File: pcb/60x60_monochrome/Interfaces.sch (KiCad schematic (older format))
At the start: 16 parts, among them J1 Conn_01x05, J10 Conn_01x01_Female, J11 Conn_01x01_Female, J12 Conn_01x01_Female, J13 Conn_01x01_Female, J14 Conn_01x02, J15 Conn_01x04, J2 Conn_01x05, J3 USB_OTG, J4 Conn_01x05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

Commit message: - add pins to the sheets, add reset/boot circuit
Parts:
- D3: footprint Diodes_SMD:D_SOD-123 -> kicad_libraries_new:badger_D_SOD-123_hand
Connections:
- wire segments 65 -> 64
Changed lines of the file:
@@
 I2C_SCL
 $Comp
-L VCC #PWR30
+L VCC #PWR033
 U 1 1 5BD6FE4D
 P 3150 2200
-F 0 "#PWR30" H 3150 2050 50  0001 C CNN
+F 0 "#PWR033" H 3150 2050 50  0001 C CNN
 F 1 "VCC" H 3150 2350 50  0000 C CNN
 F 2 "" H 3150 2200 50  0001 C CNN
@@
 Text Label 4050 2250 3    60   ~ 0
 UART_RX4
-Text Label 3450 2300 3    60   ~ 0
+Text Label 3450 2250 3    60   ~ 0
 UART_TX4
 $Comp
@@
 	3550 2100 3550 2650
 $Comp
-L GND #PWR32
+L GND #PWR034
 U 1 1 5BD6FE74
 P 4300 2150
-F 0 "#PWR32" H 4300 1900 50  0001 C CNN
+F 0 "#PWR034" H 4300 1900 50  0001 C CNN
 F 1 "GND" H 4300 2000 50  0000 C CNN
 F 2 "" H 4300 2150 50  0001 C CNN
@@
 I2C_SCL
 $Comp
-L VCC #PWR31
+L VCC #PWR035
 U 1 1 5BD7123B
 P 3300 5000
-F 0 "#PWR31" H 3300 4850 50  0001 C CNN
+F 0 "#PWR035" H 3300 4850 50  0001 C CNN
 F 1 "VCC" H 3300 5150 50  0000 C CNN
 F 2 "" H 3300 5000 50  0001 C CNN
@@
 	4100 5100 4100 4550
 $Comp
-L GND #PWR33
+L GND #PWR036
 U 1 1 5BD71262
 P 4450 5050
-F 0 "#PWR33" H 4450 4800 50  0001 C CNN
+F 0 "#PWR036" H 4450 4800 50  0001 C CNN
 F 1 "GND" H 4450 4900 50  0000 C CNN
 F 2 "" H 4450 5050 50  0001 C CNN
@@
 	0    -1   -1   0
 $EndComp
-Text Label 5250 3350 2    60   ~ 0
+Text Label 5200 3350 2    60   ~ 0
 UART_TX1
-Text Label 5250 3950 2    60   ~ 0
+Text Label 5200 3950 2    60   ~ 0
 UART_RX1
 Text Label 5250 3550 2    60   ~ 0
 I2C_SCL
 $Comp
-L VCC #PWR34
+L VCC #PWR037
 U 1 1 5BD71F25
 P 5300 4250
-F 0 "#PWR34" H 5300 4100 50  0001 C CNN
+F 0 "#PWR037" H 5300 4100 50  0001 C CNN
 F 1 "VCC" H 5300 4400 50  0000 C CNN
 F 2 "" H 5300 4250 50  0001 C CNN
@@
 	-1   0    0    1
 $EndComp
-Text Label 5250 3750 2    60   ~ 0
+Text Label 5150 3750 2    60   ~ 0
 I2C_SDA
 Text Label 2350 3300 0    60   ~ 0
@@
 I2C_SCL
 $Comp
-L VCC #PWR29
+L VCC #PWR038
 U 1 1 5BD71F2F
 P 2300 4200
-F 0 "#PWR29" H 2300 4050 50  0001 C CNN
+F 0 "#PWR038" H 2300 4050 50  0001 C CNN
 F 1 "VCC" H 2300 4350 50  0000 C CNN
 F 2 "" H 2300 4200 50  0001 C CNN
@@
 	5400 3550 4850 3550
 Wire Wire Line
-	5400 3350 4850 3350
+	4650 3350 5400 3350
 Wire Wire Line
 	5400 3150 5350 3150
@@
 Connection ~ 5300 4050
 Wire Wire Line
-	5400 3950 4850 3950
-Wire Wire Line
-	5400 3750 4850 3750
+	4700 3950 5400 3950
+Wire Wire Line
+	4600 3750 5400 3750
 Wire Wire Line
 	2200 3500 2750 3500
@@
 	5400 3850 4850 3850
 Wire Wire Line
-	5400 3450 4900 3450
-Wire Wire Line
-	4900 3450 4900 3500
-$Comp
-L GND #PWR35
+	4750 3450 5400 3450
+$Comp
+L GND #PWR039
 U 1 1 5BD71F73
 P 5350 3100
-F 0 "#PWR35" H 5350 2850 50  0001 C CNN
+F 0 "#PWR039" H 5350 2850 50  0001 C CNN
 F 1 "GND" H 5350 2950 50  0000 C CNN
 F 2 "" H 5350 3100 50  0001 C CNN
@@
 $EndComp
 $Comp
-L GND #PWR28
+L GND #PWR040
 U 1 1 5BD71F79
 P 2250 3050
-F 0 "#PWR28" H 2250 2800 50  0001 C CNN
+F 0 "#PWR040" H 2250 2800 50  0001 C CNN
 F 1 "GND" H 2250 2900 50  0000 C CNN
 F 2 "" H 2250 3050 50  0001 C CNN
@@
 F 0 "D3" H 9800 1750 50  0000 C CNN
 F 1 "Shottky" H 9800 1550 50  0000 C CNN
-F 2 "Diodes_SMD:D_SOD-123" H 9800 1650 50  0001 C CNN
+F 2 "kicad_libraries_new:badger_D_SOD-123_hand" H 9800 1650 50  0001 C CNN
 F 3 "" H 9800 1650 50  0000 C CNN
 	1    9800 1650
 	-1   0    0    1
 $EndComp
-Text Label 9750 1850 0    60   ~ 0
-USB_DP
-Text Label 9750 1950 0    60   ~ 0
-USB_DM
-$Comp
-L +5V #PWR37
+$Comp
+L +5V #PWR041
 U 1 1 5BD73B57
 P 10000 1600
-F 0 "#PWR37" H 10000 1450 50  0001 C CNN
+F 0 "#PWR041" H 10000 1450 50  0001 C CNN
 F 1 "+5V" H 10000 1740 50  0000 C CNN
 F 2 "" H 10000 1600 50  0001 C CNN
@@
 $EndComp
 $Comp
-L +3.3V #PWR38
+L +3.3V #PWR042
 U 1 1 5BD73B6C
 P 9600 3100
-F 0 "#PWR38" H 9600 2950 50  0001 C CNN
+F 0 "#PWR042" H 9600 2950 50  0001 C CNN
 F 1 "+3.3V" H 9600 3240 50  0000 C CNN
 F 2 "" H 9600 3100 50  0001 C CNN
@@
 	9600 3200 9600 3100
 $Comp
-L GND #PWR39
+L GND #PWR043
 U 1 1 5BD73B83
 P 9500 4150
-F 0 "#PWR39" H 9500 3900 50  0001 C CNN
+F 0 "#PWR043" H 9500 3900 50  0001 C CNN
 F 1 "GND" H 9500 4000 50  0000 C CNN
 F 2 "" H 9500 4150 50  0001 C CNN
@@
 $EndComp
 $Comp
-L GND #PWR36
+L GND #PWR044
 U 1 1 5BD73B89
 P 9300 2350
-F 0 "#PWR36" H 9300 2100 50  0001 C CNN
+F 0 "#PWR044" H 9300 2100 50  0001 C CNN
 F 1 "GND" H 9300 2200 50  0000 C CNN
 F 2 "" H 9300 2350 50  0001 C CNN
@@
 	1    0    0    -1
 $EndComp
+Text HLabel 4650 3350 0    60   Input ~ 0
+UART_TX1
+Text HLabel 2750 3900 2    60   Input ~ 0
+UART_TX3
+Text HLabel 2750 3300 2    60   Input ~ 0
+UART_RX3
+Text HLabel 4700 3950 0    60   Input ~ 0
+UART_RX1
+Text HLabel 4200 4550 1    60   Input ~ 0
+UART_TX2
+Text HLabel 3600 4550 1    60   Input ~ 0
+UART_RX2
+Text HLabel 4050 2650 3    60   Input ~ 0
+UART_TX4
+Text HLabel 3450 2650 3    60   Input ~ 0
+UART_RX4
+Text HLabel 4600 3750 0    60   Input ~ 0
+I2C_SDA
+Text HLabel 4850 3550 0    60   Input ~ 0
+I2C_SCL
+Text HLabel 10100 1950 2    60   Input ~ 0
+USB_DM
+Text HLabel 10100 1850 2    60   Input ~ 0
+USB_DP
+Text HLabel 3950 2600 3    60   Input ~ 0
+BTN0
+Text HLabel 3700 4600 1    60   Input ~ 0
+BTN1
+Text HLabel 4100 4550 1    60   Input ~ 0
+IN0P
+Text HLabel 2700 3800 2    60   Input ~ 0
+IN1P
+Text HLabel 4850 3850 0    60   Input ~ 0
+IN2
+Text HLabel 2750 3400 2    60   Input ~ 0
+IN3
+Text HLabel 9850 3800 2    60   Input ~ 0
+NRST
+Text HLabel 9850 3900 2    60   Input ~ 0
+SWDIO
+Text HLabel 9850 4000 2    60   Input ~ 0
+SWCLK
+Text HLabel 9850 3300 2    60   Input ~ 0
+BOOT0
 $EndSCHEMATC

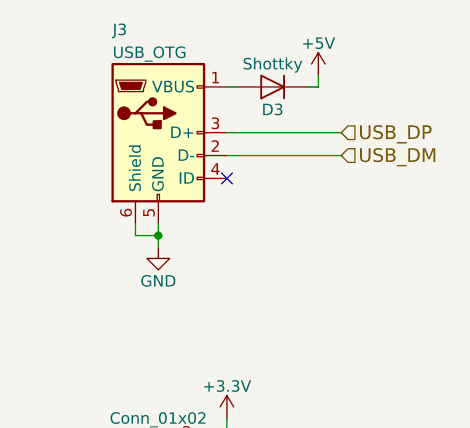
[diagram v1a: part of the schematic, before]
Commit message: - fix USB lines
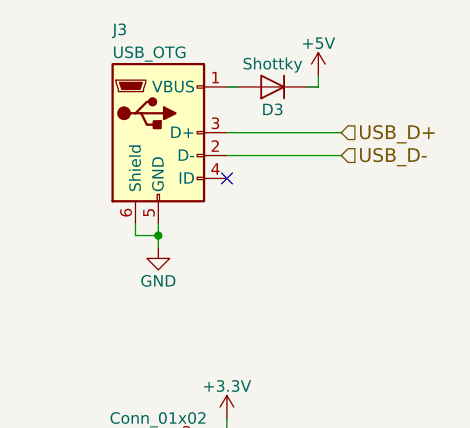
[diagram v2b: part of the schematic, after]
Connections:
- net labels added: USB_D+, USB_D-
- net labels removed: USB_DM, USB_DP
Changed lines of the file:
@@
 LIBS:contrib
 LIBS:valves
-LIBS:badger_ir2301
-LIBS:badger_mosfet_sot669
-LIBS:badger_zxct1110
 LIBS:stm32
 LIBS:74xgxx
@@
 LIBS:Xicor
 LIBS:Zilog
-LIBS:badger_dualmosfet_DMC2038LVT
-LIBS:wt51822-s4at
-LIBS:badger_resonator
-LIBS:LED_MATRIX_ysm-2388crgbc
-LIBS:badger_dm163_LED_DRIVER
-LIBS:badger_led_matrix_8x8
-LIBS:badger_m54564fp
-LIBS:badger_npic6c595
 LIBS:bcl4v2-cache
 EELAYER 25 0
@@
 I2C_SCL
 Text HLabel 10100 1950 2    60   Input ~ 0
-USB_DM
+USB_D-
 Text HLabel 10100 1850 2    60   Input ~ 0
-USB_DP
+USB_D+
 Text HLabel 3950 2600 3    60   Input ~ 0
 BTN0

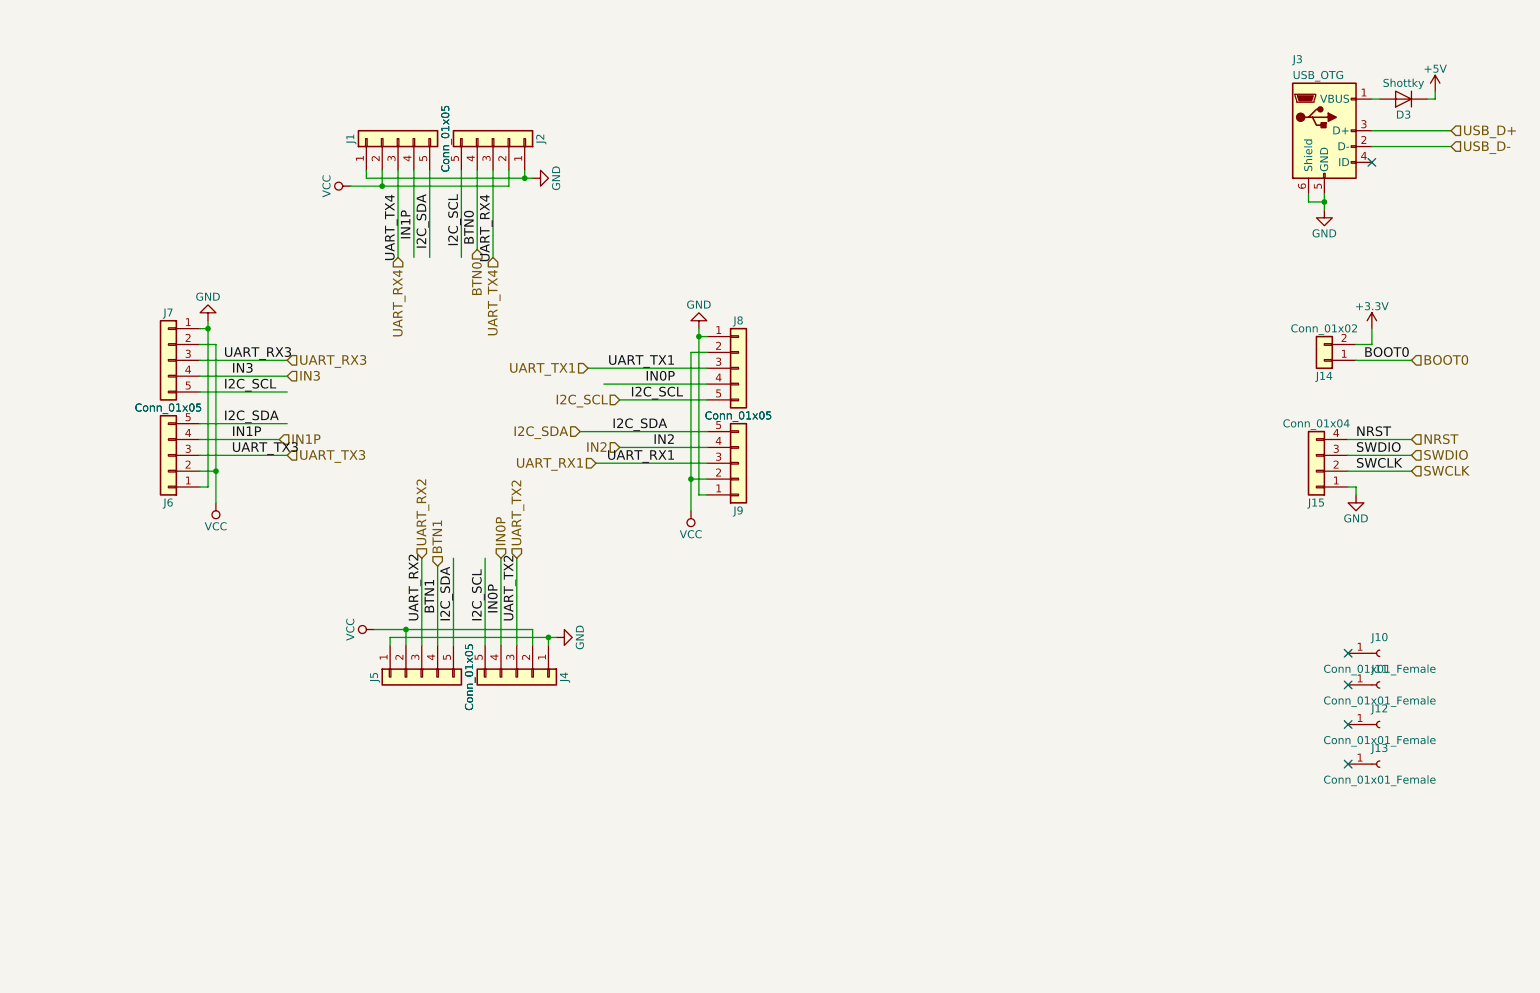
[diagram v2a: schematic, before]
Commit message: - replaced protection LEDs with mosfet
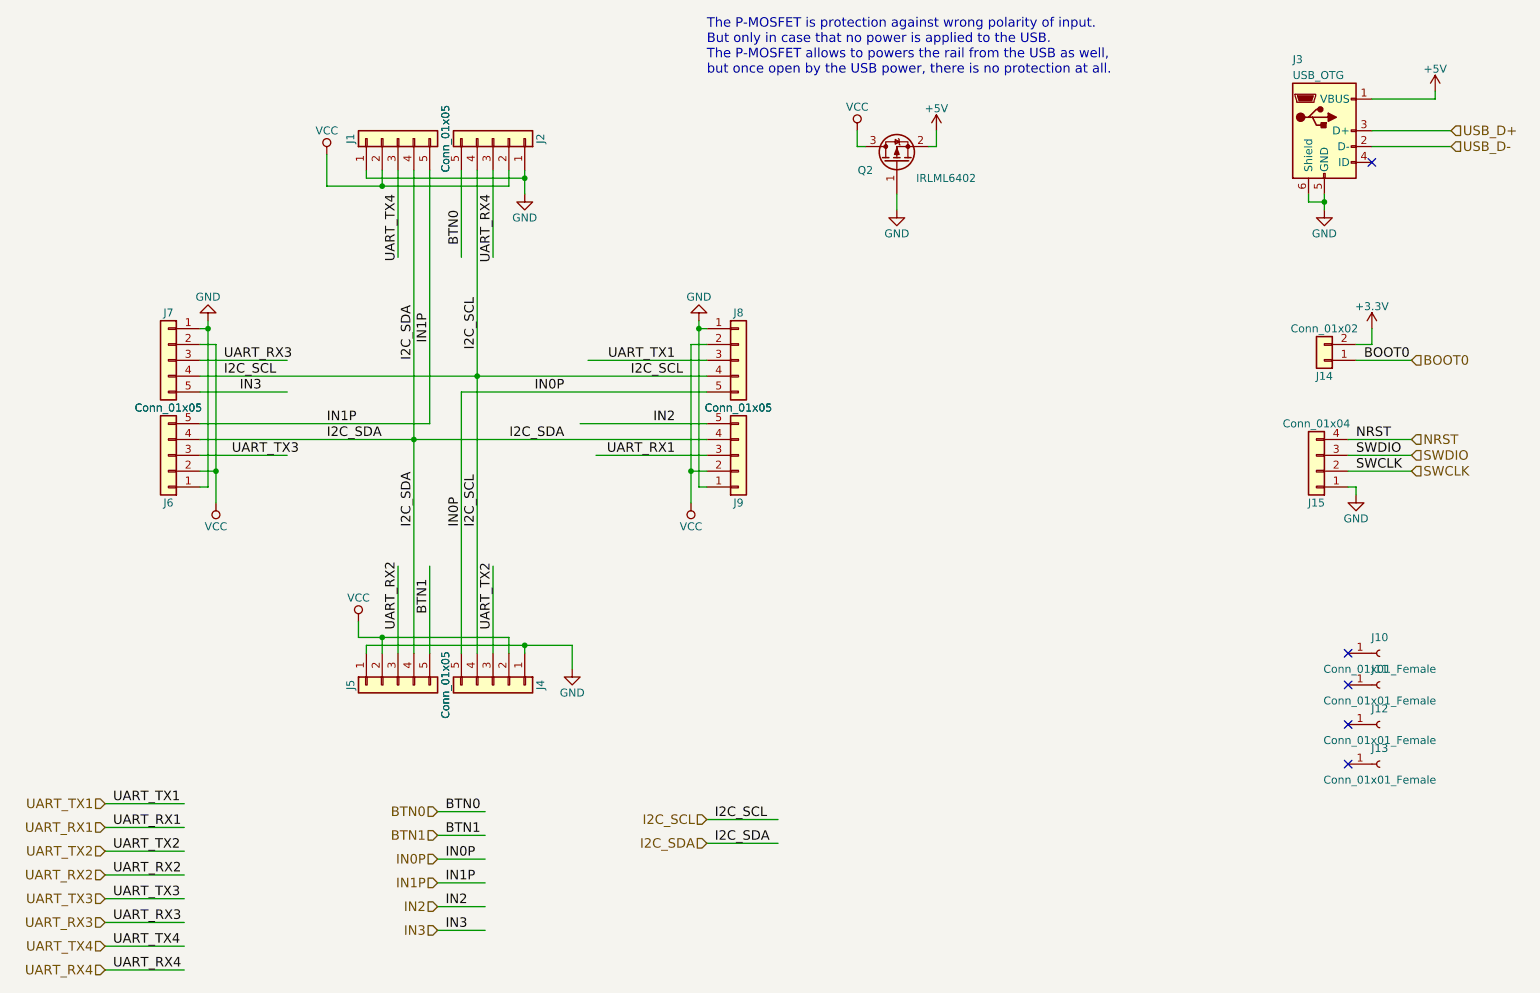
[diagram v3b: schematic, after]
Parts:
- removed D3: Shottky, kicad_libraries_new:badger_D_SOD-123_hand, symbol D
- added Q2: IRLML6402, symbol Q_PMOS_GSD
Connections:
- wire segments 64 -> 83
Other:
- note added: "The P-MOSFET is protection against wrong polarity of input.\nBut only in case that no power is applied to the USB.\nThe P-MOSFET allows to powers the rail from the USB as well,\nbut once open by the USB power, there is no protection at all."
- moved on the sheet: J4, J5, J8, J9

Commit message: - fix some footprints to reduce ERC errors
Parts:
- Q2: footprint (none) -> kicad_libraries_new:badger_SOT-23_handsolder
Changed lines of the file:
@@
 EESchema Schematic File Version 2
+LIBS:bcl4v2-rescue
 LIBS:power
 LIBS:device
@@
 I2C_SCL
 $Comp
-L VCC #PWR033
+L VCC #PWR031
 U 1 1 5BD6FE4D
 P 3000 2000
-F 0 "#PWR033" H 3000 1850 50  0001 C CNN
+F 0 "#PWR031" H 3000 1850 50  0001 C CNN
 F 1 "VCC" H 3000 2150 50  0000 C CNN
 F 2 "" H 3000 2000 50  0001 C CNN
@@
 BTN0
 $Comp
-L GND #PWR034
+L GND #PWR032
 U 1 1 5BD6FE74
 P 4250 2250
-F 0 "#PWR034" H 4250 2000 50  0001 C CNN
+F 0 "#PWR032" H 4250 2000 50  0001 C CNN
 F 1 "GND" H 4250 2100 50  0000 C CNN
 F 2 "" H 4250 2250 50  0001 C CNN
@@
 I2C_SCL
 $Comp
-L VCC #PWR035
+L VCC #PWR033
 U 1 1 5BD7123B
 P 3200 4950
-F 0 "#PWR035" H 3200 4800 50  0001 C CNN
+F 0 "#PWR033" H 3200 4800 50  0001 C CNN
 F 1 "VCC" H 3200 5100 50  0000 C CNN
 F 2 "" H 3200 4950 50  0001 C CNN
@@
 BTN1
 $Comp
-L GND #PWR036
+L GND #PWR034
 U 1 1 5BD71262
 P 4550 5250
-F 0 "#PWR036" H 4550 5000 50  0001 C CNN
+F 0 "#PWR034" H 4550 5000 50  0001 C CNN
 F 1 "GND" H 4550 5100 50  0000 C CNN
 F 2 "" H 4550 5250 50  0001 C CNN
@@
 I2C_SCL
 $Comp
-L VCC #PWR037
+L VCC #PWR035
 U 1 1 5BD71F25
 P 5300 4200
-F 0 "#PWR037" H 5300 4050 50  0001 C CNN
+F 0 "#PWR035" H 5300 4050 50  0001 C CNN
 F 1 "VCC" H 5300 4350 50  0000 C CNN
 F 2 "" H 5300 4200 50  0001 C CNN
@@
 I2C_SCL
 $Comp
-L VCC #PWR038
+L VCC #PWR036
 U 1 1 5BD71F2F
 P 2300 4200
-F 0 "#PWR038" H 2300 4050 50  0001 C CNN
+F 0 "#PWR036" H 2300 4050 50  0001 C CNN
 F 1 "VCC" H 2300 4350 50  0000 C CNN
 F 2 "" H 2300 4200 50  0001 C CNN
@@
 IN2
 $Comp
-L GND #PWR039
+L GND #PWR037
 U 1 1 5BD71F73
 P 5350 3050
-F 0 "#PWR039" H 5350 2800 50  0001 C CNN
+F 0 "#PWR037" H 5350 2800 50  0001 C CNN
 F 1 "GND" H 5350 2900 50  0000 C CNN
 F 2 "" H 5350 3050 50  0001 C CNN
@@
 $EndComp
 $Comp
-L GND #PWR040
+L GND #PWR038
 U 1 1 5BD71F79
 P 2250 3050
-F 0 "#PWR040" H 2250 2800 50  0001 C CNN
+F 0 "#PWR038" H 2250 2800 50  0001 C CNN
 F 1 "GND" H 2250 2900 50  0000 C CNN
 F 2 "" H 2250 3050 50  0001 C CNN
@@
 NoConn ~ 9600 2050
 $Comp
-L +5V #PWR041
+L +5V #PWR039
 U 1 1 5BD73B57
 P 10000 1600
-F 0 "#PWR041" H 10000 1450 50  0001 C CNN
+F 0 "#PWR039" H 10000 1450 50  0001 C CNN
 F 1 "+5V" H 10000 1740 50  0000 C CNN
 F 2 "" H 10000 1600 50  0001 C CNN
@@
 $EndComp
 $Comp
-L +3.3V #PWR042
+L +3.3V #PWR040
 U 1 1 5BD73B6C
 P 9600 3100
-F 0 "#PWR042" H 9600 2950 50  0001 C CNN
+F 0 "#PWR040" H 9600 2950 50  0001 C CNN
 F 1 "+3.3V" H 9600 3240 50  0000 C CNN
 F 2 "" H 9600 3100 50  0001 C CNN
@@
 $EndComp
 $Comp
-L GND #PWR043
+L GND #PWR041
 U 1 1 5BD73B83
 P 9500 4150
-F 0 "#PWR043" H 9500 3900 50  0001 C CNN
+F 0 "#PWR041" H 9500 3900 50  0001 C CNN
 F 1 "GND" H 9500 4000 50  0000 C CNN
 F 2 "" H 9500 4150 50  0001 C CNN
@@
 $EndComp
 $Comp
-L GND #PWR044
+L GND #PWR042
 U 1 1 5BD73B89
 P 9300 2350
-F 0 "#PWR044" H 9300 2100 50  0001 C CNN
+F 0 "#PWR042" H 9300 2100 50  0001 C CNN
 F 1 "GND" H 9300 2200 50  0000 C CNN
 F 2 "" H 9300 2350 50  0001 C CNN
@@
 BOOT0
 $Comp
-L +5V #PWR045
+L +5V #PWR043
 U 1 1 5BDD7179
 P 6850 1850
-F 0 "#PWR045" H 6850 1700 50  0001 C CNN
+F 0 "#PWR043" H 6850 1700 50  0001 C CNN
 F 1 "+5V" H 6850 1990 50  0000 C CNN
 F 2 "" H 6850 1850 50  0001 C CNN
@@
 $EndComp
 $Comp
-L VCC #PWR046
+L VCC #PWR044
 U 1 1 5BDD717F
 P 6350 1850
-F 0 "#PWR046" H 6350 1700 50  0001 C CNN
+F 0 "#PWR044" H 6350 1700 50  0001 C CNN
 F 1 "VCC" H 6350 2000 50  0000 C CNN
 F 2 "" H 6350 1850 50  0001 C CNN
@@
 F 0 "Q2" V 6550 2200 50  0000 L CNN
 F 1 "IRLML6402" V 6500 1550 50  0000 L CNN
-F 2 "" H 6800 2150 50  0001 C CNN
+F 2 "kicad_libraries_new:badger_SOT-23_handsolder" H 6800 2150 50  0001 C CNN
 F 3 "" H 6600 2050 50  0001 C CNN
 	1    6600 2050
@@
 $EndComp
 $Comp
-L GND #PWR047
+L GND #PWR045
 U 1 1 5BDD7A19
 P 6600 2350
-F 0 "#PWR047" H 6600 2100 50  0001 C CNN
+F 0 "#PWR045" H 6600 2100 50  0001 C CNN
 F 1 "GND" H 6600 2200 50  0000 C CNN
 F 2 "" H 6600 2350 50  0001 C CNN
